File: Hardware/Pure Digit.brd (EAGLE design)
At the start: 19.3 x 100 mm, 46 parts, among them IC1 BA178M05FP, IC3 TL074, IC4 ATMEGA328P, IC5 MCP3202, IC6 MCP4921, Q1 20MHz, SW1 ROTARTY_ENCODER

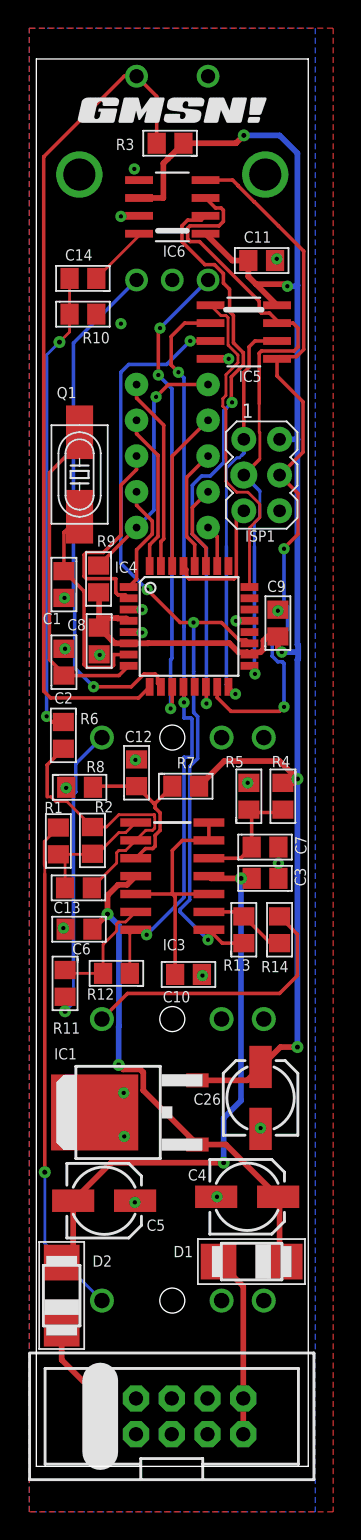
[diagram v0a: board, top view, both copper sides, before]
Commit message: Digit 2.0
Digit Updated to V2.0 28/4/21

RC filter added to DAC output.
Cap added to output opamp.
SD Card Reader added.

To do: Replace power so 5V comes from case power supply, inline with low noise techniques. May require complete redesign.
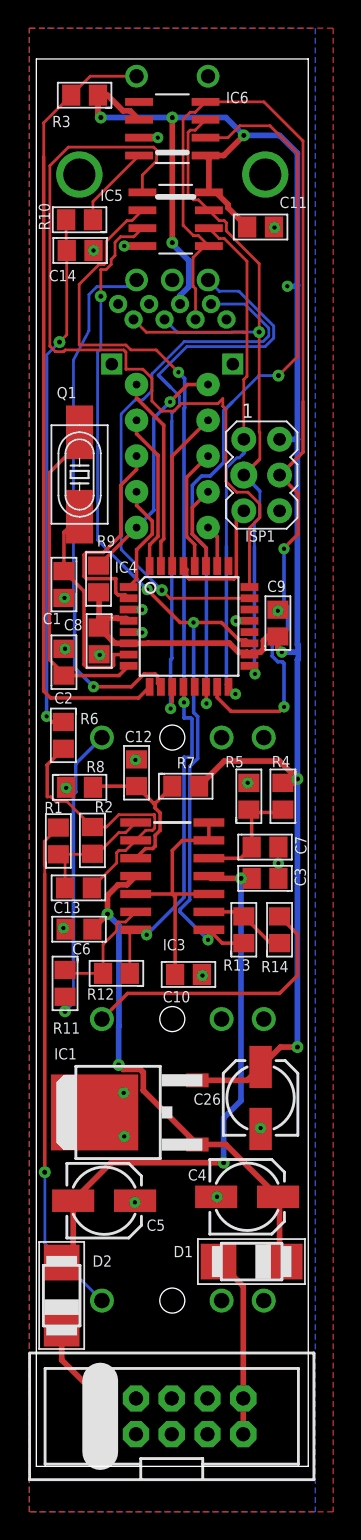
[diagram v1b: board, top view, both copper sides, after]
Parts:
- removed U$2: (no value), gmsnLogo:GMSN!_LOGO
- added U$3: SOCKET_SD_CARD_VERTICAL, GMSN:PJS008U-3000
- moved IC5 9.37 mm to (10.4, 107.1)
- moved R3 6.97 mm to (3.93, 115.9)
- moved IC6 5.56 mm to (10.2, 113.5)
- moved C14 4.53 mm to (3.61, 104.9)
- moved R10 4.17 mm to (3.57, 107.0)
- moved C11 2.38 mm to (16.4, 106.5)
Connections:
- new net CS3: IC4.23, U$3.P$2
- net 5V: now also U$3.P$4
- net GND: now also U$3.GND1, U$3.GND2, U$3.P$6
- net MISO: now also U$3.P$7
- net MOSI: now also U$3.P$3
- net SCK: now also U$3.P$5
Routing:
- net CS3: track 0.00 -> 39.0 mm, vias 0 -> 1
- net CS2: track 23.3 -> 56.0 mm
- net MOSI: track 52.5 -> 75.0 mm
- net 5V: track 130.2 -> 149.2 mm, vias 5 -> 8
- net MISO: track 28.6 -> 44.6 mm
- net CV_IN1: track 53.6 -> 67.4 mm
- net CS1: track 41.7 -> 52.7 mm
- net ENCA: track 33.9 -> 42.3 mm, vias 3 -> 1
- net CV_IN2: track 59.9 -> 65.6 mm
- net SCK: track 46.2 -> 51.9 mm, vias 1 -> 2
- net N$6: track 33.1 -> 37.2 mm
- net SW: track 60.3 -> 56.4 mm
- net N$14: track 4.43 -> 5.92 mm
- net ENCB: track 37.2 -> 38.4 mm
- net N$13: track 17.7 -> 16.9 mm
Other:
- board text added: "Pure Digit v2.0 cc-by 4.0 2021 The Little Red Hen"
- board text removed: "Pure Digit v1.1 cc-by 4.0 2021 The Little Red Hen"
